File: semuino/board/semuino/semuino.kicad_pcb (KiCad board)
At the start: 2 copper layers, 115 x 77 mm, 34 parts, among them J1 bpc_pwr_10A, J10 Conn_01x02, J11 Conn_01x02, J12 Conn_01x02, J13 Conn_01x02, J2 bpc_pwr_10A, J3 bpc_pwr_5A, J4 bpc_pwr_5A, J5 bpc_pwr_5A, J6 bpc_pwr_5A, J7 Conn_01x03, J8 Conn_01x03, J9 Conn_01x03, Q1 TIP41C, Q2 TIP41C, Q3 TIP41C, Q4 TIP41C

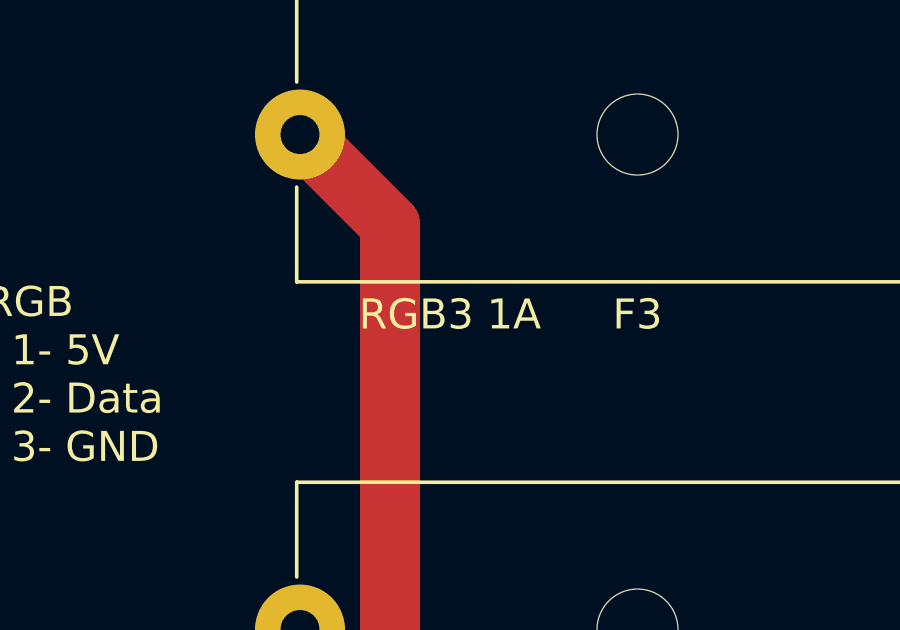
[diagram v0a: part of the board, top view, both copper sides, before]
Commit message: Erreur marquage fusible
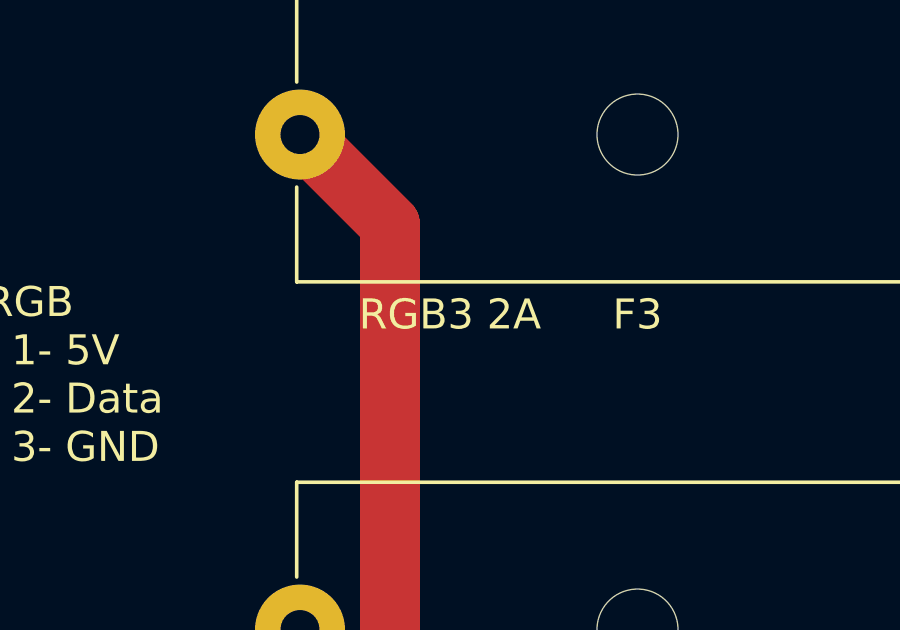
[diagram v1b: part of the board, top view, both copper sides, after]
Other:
- board text removed: "RGB3 1A"

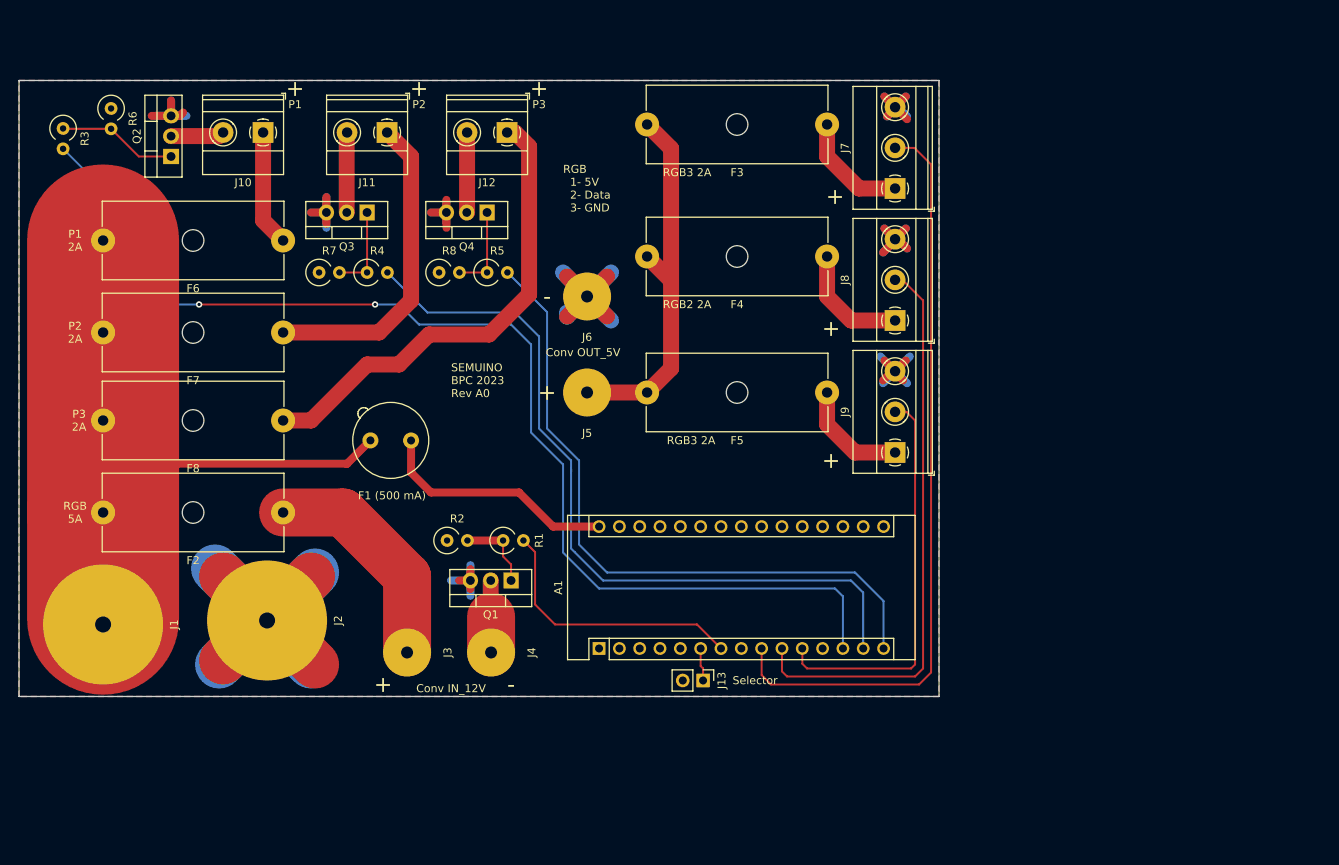
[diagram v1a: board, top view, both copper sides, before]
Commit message: Carte de commande éclairage semi
- Alim 12V/10A
- 3 sorties 12V/2A
- 3 sorties RGB 5V/2A
- RTC
- Sonde température
- extension ESP 01 Wifi
- 1 entrée select
- 1 entrée ON/OFF pour ESP 01
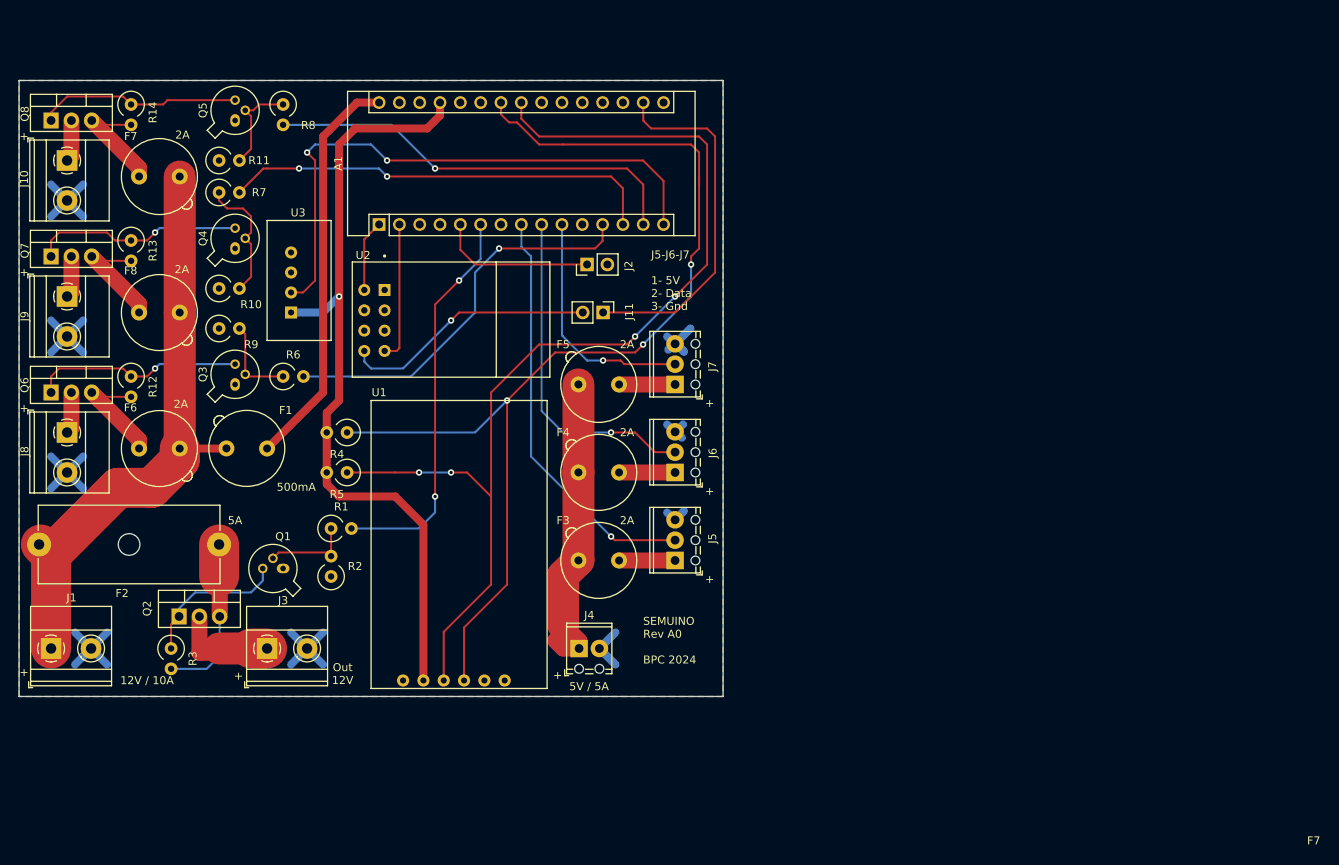
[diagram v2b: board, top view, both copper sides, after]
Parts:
- removed F1 (500 mA): 500mA, Fuse:Fuseholder_TR5_Littelfuse_No560_No460
- removed J12: Conn_01x02, TerminalBlock_Phoenix:TerminalBlock_Phoenix_MKDS-1,5-2_1x02_P5.00mm_Horizontal
- removed J13: Conn_01x02, Connector_PinHeader_2.54mm:PinHeader_1x02_P2.54mm_Vertical
- added ?: , , F.Cu at (88.8, 66.0)
- added F1: 500mA, Fuse:Fuseholder_TR5_Littelfuse_No560_No460, F.Cu at (106.0, 105.0)
- added Q5: 2N2222A, Package_TO_SOT_THT:TO-18-3, F.Cu at (102.0, 64.0)
- added Q6: P03P4L-04, Package_TO_SOT_THT:TO-220-3_Vertical, F.Cu at (79.0, 98.0)
- added Q7: P03P4L-04, Package_TO_SOT_THT:TO-220-3_Vertical, F.Cu at (79.0, 81.0)
- added Q8: P03P4L-04, Package_TO_SOT_THT:TO-220-3_Vertical, F.Cu at (79.0, 64.0)
- added R10: 100k, Resistor_THT:R_Axial_DIN0309_L9.0mm_D3.2mm_P2.54mm_Vertical, F.Cu at (100.0, 85.0)
- added R11: 100k, Resistor_THT:R_Axial_DIN0309_L9.0mm_D3.2mm_P2.54mm_Vertical, F.Cu at (100.0, 69.0)
- added R12: 100, Resistor_THT:R_Axial_DIN0309_L9.0mm_D3.2mm_P2.54mm_Vertical, F.Cu at (89.0, 96.0)
- added R13: 100k, Resistor_THT:R_Axial_DIN0309_L9.0mm_D3.2mm_P2.54mm_Vertical, F.Cu at (89.0, 79.0)
- added R14: 100k, Resistor_THT:R_Axial_DIN0309_L9.0mm_D3.2mm_P2.54mm_Vertical, F.Cu at (89.0, 62.0)
- added R9: 100k, Resistor_THT:R_Axial_DIN0309_L9.0mm_D3.2mm_P2.54mm_Vertical, F.Cu at (100.0, 90.0)
- added U1: RtcArduino, bpc:BPC_RtcArduino, F.Cu at (123.0, 134.0)
- added U2: BPC_ESP8266-01_ESP-01, bpc:BPC_XCVR_ESP8266-01_ESP-01, F.Cu at (129.0, 89.0)
- added U3: BPC_DHT22, bpc:BPC_DHT22, F.Cu at (109.0, 88.0)
- A1: value Arduino_Nano_v3.x -> Arduino_Nano_v2.x
- F3, F4, F5, F6, F7, F8: footprint Fuse:Fuseholder_Cylinder-5x20mm_Schurter_0031_8201_Horizontal_Open -> Fuse:Fuseholder_TR5_Littelfuse_No560_No460
- J1: value bpc_pwr_10A -> Conn_01x02; footprint bpc:BPC_PWR_10A -> TerminalBlock_Phoenix:TerminalBlock_Phoenix_MKDS-1,5-2_1x02_P5.00mm_Horizontal
- J11: footprint TerminalBlock_Phoenix:TerminalBlock_Phoenix_MKDS-1,5-2_1x02_P5.00mm_Horizontal -> Connector_PinHeader_2.54mm:PinHeader_1x02_P2.54mm_Vertical
- J2: value bpc_pwr_10A -> Conn_01x02; footprint bpc:BPC_PWR_10A -> Connector_PinHeader_2.54mm:PinHeader_1x02_P2.54mm_Vertical
- J3: value bpc_pwr_5A -> Conn_01x02; footprint bpc:BPC_PWR_5A -> TerminalBlock_Phoenix:TerminalBlock_Phoenix_MKDS-1,5-2_1x02_P5.00mm_Horizontal
- J4: value bpc_pwr_5A -> Conn_01x02; footprint bpc:BPC_PWR_5A -> TerminalBlock_Phoenix:TerminalBlock_Phoenix_MPT-0,5-2-2.54_1x02_P2.54mm_Horizontal
- J5, J6: value bpc_pwr_5A -> Conn_01x03; footprint bpc:BPC_PWR_5A -> TerminalBlock_Phoenix:TerminalBlock_Phoenix_MPT-0,5-3-2.54_1x03_P2.54mm_Horizontal
- J7: footprint TerminalBlock_Phoenix:TerminalBlock_Phoenix_MKDS-1,5-3-5.08_1x03_P5.08mm_Horizontal -> TerminalBlock_Phoenix:TerminalBlock_Phoenix_MPT-0,5-3-2.54_1x03_P2.54mm_Horizontal
- J8, J9: value Conn_01x03 -> Conn_01x02; footprint TerminalBlock_Phoenix:TerminalBlock_Phoenix_MKDS-1,5-3-5.08_1x03_P5.08mm_Horizontal -> TerminalBlock_Phoenix:TerminalBlock_Phoenix_MKDS-1,5-2_1x02_P5.00mm_Horizontal
- Q1, Q3, Q4: value TIP41C -> 2N2222A; footprint Package_TO_SOT_THT:TO-220-3_Vertical -> Package_TO_SOT_THT:TO-18-3
- Q2: value TIP41C -> P03P4L-04
- R1: value 50 -> 100
- R3, R4, R5: value 100 -> 100k
- R6, R7, R8: value 100k -> 100
- moved J9 105.3 mm to (81.0, 86.0), turned to 270 degrees
- moved J8 104.4 mm to (81.0, 103.0), turned to 270 degrees
- moved R3 66.4 mm to (94.0, 130.0)
- moved F3 60.4 mm to (150.0, 119.0)
- moved J2 59.8 mm to (146.0, 82.0)
- moved A1 59.7 mm to (120.0, 77.0)
- moved Q2 57.5 mm to (95.0, 126.0), turned to 0 degrees
- moved R6 39.8 mm to (108.0, 96.0), turned to 0 degrees
- moved F4 37.5 mm to (150.0, 108.0)
- moved J7 36.8 mm to (157.0, 97.0)
- moved J11 35.1 mm to (148.0, 88.0), turned to 270 degrees
- moved Q4 31.8 mm to (102.0, 80.0), turned to 90 degrees
- moved F6 31.6 mm to (90.0, 105.0), turned to 0 degrees
- moved R5 30.5 mm to (116.0, 108.0), turned to 180 degrees
- moved R8 28.7 mm to (108.0, 62.0), turned to 270 degrees
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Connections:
- A1 pad 1: Net-(A1-Pad1) -> NanoTx
- A1 pad 10: CmdRGB2 -> CmdRGB3
- A1 pad 11: CmdRGB3 -> Net-(A1-Pad11)
- A1 pad 12: Net-(A1-Pad12) -> CmdP1
- A1 pad 13: CmdP1 -> CmdP2
- A1 pad 14: CmdP2 -> CmdP3
- A1 pad 15: CmdP3 -> Temp
- A1 pad 17: Net-(A1-Pad17) -> 3.3V
- A1 pad 2: Net-(A1-Pad2) -> NanoRX
- A1 pad 23: Net-(A1-Pad23) -> SDA
- A1 pad 24: Net-(A1-Pad24) -> SCL
- A1 pad 27: Net-(A1-Pad27) -> Vcc
- A1 pad 30: Net-(A1-Pad30) -> Vin
- A1 pad 5: Net-(A1-Pad5) -> SELECT
- A1 pad 6: SELECT -> CmdPWR5
- A1 pad 7: CmdPWR5 -> Net-(A1-Pad7)
- A1 pad 8: Net-(A1-Pad8) -> CmdRGB1
- A1 pad 9: CmdRGB1 -> CmdRGB2
- F3 pad 2: Net-(F3-Pad2) -> PWR_5V
- F4 pad 2: Net-(F3-Pad2) -> PWR_5V
- F5 pad 2: Net-(F3-Pad2) -> PWR_5V
- J10 pad 1: Net-(F6-Pad1) -> Net-(J10-Pad1)
- J10 pad 2: Net-(J10-Pad2) -> GND
- J11 pad 1: Net-(F7-Pad1) -> 3.3V
- J2 pad 1: GND -> SELECT
- J3 pad 1: Net-(F2-Pad1) -> Net-(J3-Pad1)
- J4 pad 1: Net-(J4-Pad1) -> PWR_5V
- J5 pad 1: Net-(F3-Pad2) -> Net-(F3-Pad1)
- J6 pad 1: GND -> Net-(F4-Pad1)
- J7 pad 1: Net-(F3-Pad1) -> Net-(F5-Pad1)
- J7 pad 2: CmdRGB1 -> CmdRGB3
- J8 pad 1: Net-(F4-Pad1) -> Net-(J8-Pad1)
- J8 pad 2: CmdRGB2 -> GND
- J9 pad 1: Net-(F5-Pad1) -> Net-(J9-Pad1)
- J9 pad 2: CmdRGB3 -> GND
- Q1 pad 1: Net-(Q1-Pad1) -> GND
- Q1 pad 2: Net-(J4-Pad1) -> Net-(Q1-Pad2)
- Q1 pad 3: GND -> Net-(Q1-Pad3)
- Q2 pad 1: Net-(Q2-Pad1) -> Net-(Q1-Pad3)
- Q2 pad 2: Net-(J10-Pad2) -> Net-(J3-Pad1)
- Q2 pad 3: GND -> Net-(F2-Pad1)
- Q3 pad 1: Net-(Q3-Pad1) -> GND
- Q3 pad 2: Net-(J11-Pad2) -> Net-(Q3-Pad2)
- Q3 pad 3: GND -> Net-(Q3-Pad3)
- Q4 pad 1: Net-(Q4-Pad1) -> GND
- Q4 pad 2: Net-(J12-Pad2) -> Net-(Q4-Pad2)
- Q4 pad 3: GND -> Net-(Q4-Pad3)
- R1 pad 1: Net-(Q1-Pad1) -> Net-(Q1-Pad2)
- R2 pad 2: Net-(Q1-Pad1) -> Net-(Q1-Pad2)
- R3 pad 1: Net-(Q2-Pad1) -> Net-(Q1-Pad3)
- R3 pad 2: CmdP1 -> Net-(F2-Pad1)
- R4 pad 1: Net-(Q3-Pad1) -> SCL
- R4 pad 2: CmdP2 -> Vcc
- R5 pad 1: Net-(Q4-Pad1) -> SDA
- R5 pad 2: CmdP3 -> Vcc
- R6 pad 1: GND -> Net-(Q3-Pad2)
- R6 pad 2: Net-(Q2-Pad1) -> CmdP1
- R7 pad 1: GND -> Net-(Q4-Pad2)
- R7 pad 2: Net-(Q3-Pad1) -> CmdP2
- R8 pad 1: GND -> Net-(Q5-Pad2)
- R8 pad 2: Net-(Q4-Pad1) -> CmdP3
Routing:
- net SCL: track 0.00 -> 134.9 mm, vias 0 -> 3
- net SDA: track 0.00 -> 132.9 mm, vias 0 -> 4
- net GND: track 186.9 -> 78.7 mm
- net Vcc: track 0.00 -> 99.3 mm, vias 0 -> 1
- net CmdP1: track 143.3 -> 49.4 mm, vias 2 -> 1
- net Temp: track 0.00 -> 72.3 mm, vias 0 -> 2
- net Vin: track 0.00 -> 50.7 mm
- net Net-(F3-Pad2): track 47.7 -> 0.00 mm
- net 3.3V: track 0.00 -> 45.1 mm
- net Net-(F8-Pad1): track 59.2 -> 14.6 mm
- net CmdRGB1: track 94.5 -> 51.8 mm, vias 0 -> 1
- net CmdP2: track 96.7 -> 54.7 mm, vias 0 -> 2
- net PWR_5V: track 0.00 -> 38.0 mm
- net CmdP3: track 84.6 -> 53.1 mm, vias 0 -> 1
- net Net-(A1-Pad30): track 30.3 -> 0.00 mm
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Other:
- board size 115 x 77 mm -> 88 x 77 mm
- board text added: "12V / 10A"
- board text added: "2A"
- board text added: "500mA"
- board text added: "5A"
- board text added: "5V / 5A"
- board text added: "J5-J6-J7 1- 5V 2- Data 3- Gnd"
- board text added: "Out 12V"
- board text added: "SEMUINO Rev A0 BPC 2024"
- board text removed: "-"
- board text removed: "Conv IN_12V"
- board text removed: "Conv OUT_5V"
- board text removed: "P1"
- board text removed: "P1 2A"
- board text removed: "P2"
- board text removed: "P2 2A"
- board text removed: "P3"
- board text removed: "P3 2A"
- board text removed: "RGB 1- 5V 2- Data 3- GND"
- board text removed: "RGB 5A"
- board text removed: "RGB2 2A"
- board text removed: "RGB3 2A"
- board text removed: "SEMUINO BPC 2023 Rev A0"
- board text removed: "Selector"

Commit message: SEMUINO: Rework de la carte
- 3 LEDs 12V
- 3 LEDs RGB (avec R de protection sur data)
- 3 capteurs humidité sol
- 1 Connecteur pour écran OLED
- 1 RTC
- 1 ESP01 pour le Wifi
- Des fusibles
- carte au format boîte de dérivation
- ...
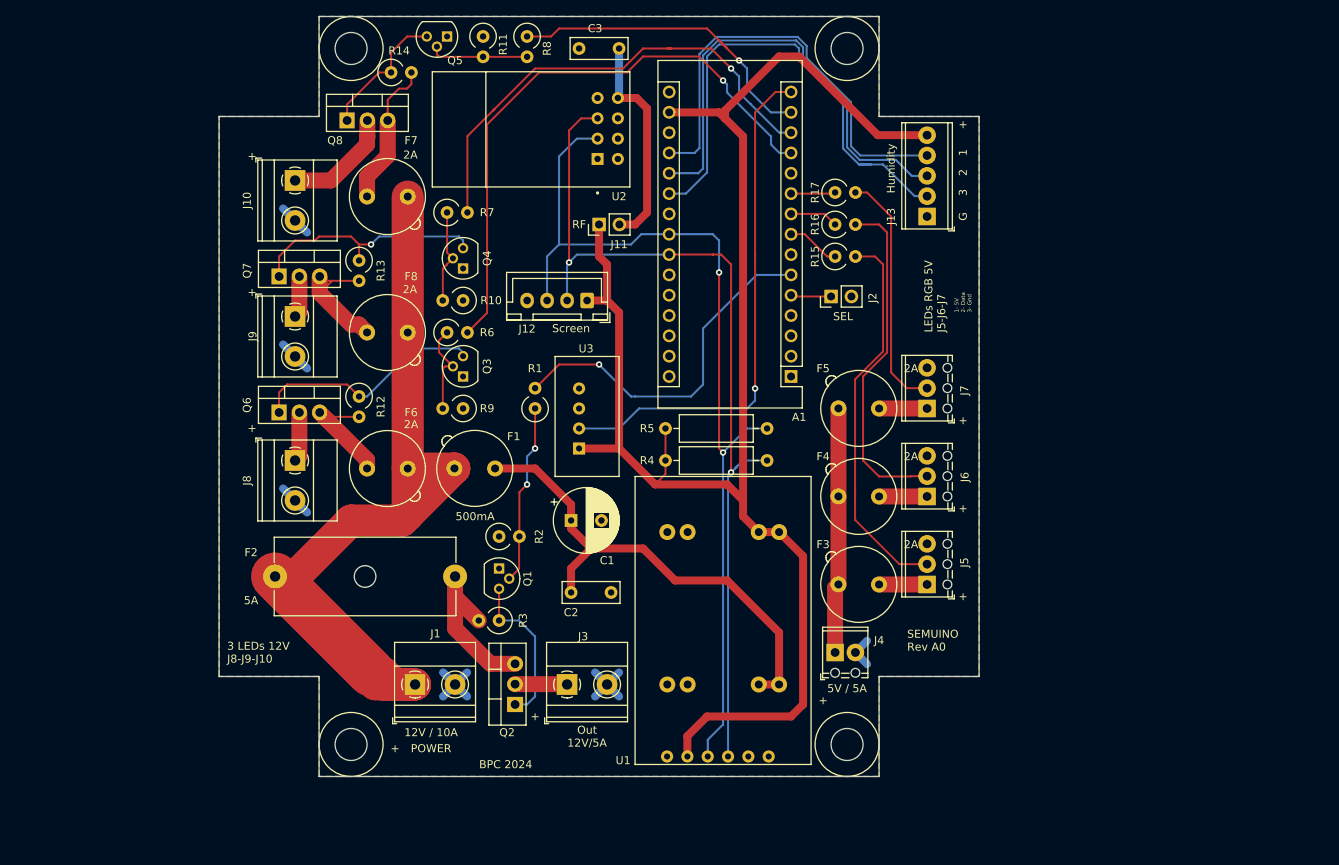
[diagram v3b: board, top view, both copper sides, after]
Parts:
- removed the ? at (88.8, 66.0)
- added ?: , , F.Cu at (193.5, 78.0)
- added ?: , , F.Cu at (193.5, 71.0)
- added ?: , , F.Cu at (57.3, 77.5)
- added C1: 20µF, Capacitor_THT:CP_Radial_D8.0mm_P3.80mm, F.Cu at (144.0, 114.0)
- added C2: 100nF, Capacitor_THT:C_Disc_D7.0mm_W2.5mm_P5.00mm, F.Cu at (144.0, 123.0)
- added C3: 100nF, Capacitor_THT:C_Disc_D7.0mm_W2.5mm_P5.00mm, F.Cu at (150.0, 55.0)
- added J12: Screen, Connector_JST:JST_XH_B4B-XH-A_1x04_P2.50mm_Vertical, F.Cu at (146.0, 86.5)
- added J13: Earth humidity sensor, TerminalBlock_Phoenix:TerminalBlock_Phoenix_MPT-0,5-5-2.54_1x05_P2.54mm_Horizontal, F.Cu at (188.5, 76.0)
- added R15: 100, Resistor_THT:R_Axial_DIN0309_L9.0mm_D3.2mm_P2.54mm_Vertical, F.Cu at (177.0, 81.0)
- added R16: 100, Resistor_THT:R_Axial_DIN0309_L9.0mm_D3.2mm_P2.54mm_Vertical, F.Cu at (177.0, 77.0)
- added R17: 100, Resistor_THT:R_Axial_DIN0309_L9.0mm_D3.2mm_P2.54mm_Vertical, F.Cu at (177.0, 73.0)
- added REF**: BPC_Trou4mm_Fixation, bpc:BPC_Trou4mm_Fixation, F.Cu at (116.5, 55.0)
- added REF**: BPC_Trou4mm_Fixation, bpc:BPC_Trou4mm_Fixation, F.Cu at (116.5, 142.0)
- added REF**: BPC_Trou4mm_Fixation, bpc:BPC_Trou4mm_Fixation, F.Cu at (178.5, 55.0)
- added REF**: BPC_Trou4mm_Fixation, bpc:BPC_Trou4mm_Fixation, F.Cu at (178.5, 142.0)
- added U4: BPC_Alim3_3V, bpc:BPC_Alim3_3V, B.Cu at (170.0, 134.5)
- J1: value Conn_01x02 -> 12V_POWER_IN
- J10: value Conn_01x02 -> POW LED 3
- J11: value Conn_01x02 -> RF ON/OFF
- J2: value Conn_01x02 -> Select
- J3: value Conn_01x02 -> 12V_POWER_OUT
- J4: value Conn_01x02 -> 5V_POWER_IN
- J5: value Conn_01x03 -> RGB 1
- J6: value Conn_01x03 -> RGB 2
- J7: value Conn_01x03 -> RGB 3
- J8: value Conn_01x02 -> POW LED 1
- J9: value Conn_01x02 -> POW LED 2
- Q1, Q3, Q4, Q5: footprint Package_TO_SOT_THT:TO-18-3 -> Package_TO_SOT_THT:TO-92
- R1, R6, R7, R8: value 100 -> 220
- R12: value 100 -> 100k
- R4, R5: value 100k -> 10k; footprint Resistor_THT:R_Axial_DIN0309_L9.0mm_D3.2mm_P2.54mm_Vertical -> Resistor_THT:R_Axial_DIN0309_L9.0mm_D3.2mm_P12.70mm_Horizontal
- moved A1 54.9 mm to (171.5, 96.0), turned to 180 degrees
- moved R5 52.8 mm to (168.5, 102.5)
- moved R4 52.6 mm to (168.5, 106.5)
- moved J1 45.7 mm to (124.5, 134.5)
- moved Q2 43.4 mm to (137.0, 137.0), turned to 90 degrees
- moved R3 41.1 mm to (135.0, 126.5), turned to 180 degrees
- moved U3 39.8 mm to (145.0, 105.0)
- moved J3 37.8 mm to (143.5, 134.5)
- moved Q8 37.0 mm to (116.0, 64.0)
- moved R11 36.5 mm to (133.0, 53.5), turned to 270 degrees
- moved U1 34.3 mm to (156.0, 143.5)
- moved R14 32.7 mm to (121.5, 58.0), turned to 0 degrees
- moved F3 32.6 mm to (182.5, 122.0)
- moved F4 32.6 mm to (182.5, 111.0)
- moved F5 32.6 mm to (182.5, 100.0)
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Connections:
- A1 pad 1: NanoTx -> Net-(A1-Pad1)
- A1 pad 19: Net-(A1-Pad19) -> Hum1
- A1 pad 2: NanoRX -> Net-(A1-Pad2)
- A1 pad 20: Net-(A1-Pad20) -> Hum2
- A1 pad 21: Net-(A1-Pad21) -> Hum3
- A1 pad 27: Vcc -> Net-(A1-Pad27)
- A1 pad 30: Vin -> Net-(A1-Pad30)
- J5 pad 2: CmdRGB1 -> Net-(J5-Pad2)
- J6 pad 2: CmdRGB2 -> Net-(J6-Pad2)
- J7 pad 2: CmdRGB3 -> Net-(J7-Pad2)
- R4 pad 2: Vcc -> 3.3V
- R5 pad 2: Vcc -> 3.3V
- R8 pad 1: Net-(Q5-Pad2) -> CmdP3
- R8 pad 2: CmdP3 -> Net-(Q5-Pad2)
- U1 pad 2: Vcc -> 3.3V
- U2 pad 2: Net-(U2-Pad2) -> SDA
- U2 pad 3: Net-(U2-Pad3) -> SCL
- U2 pad 4: NanoRX -> Net-(U2-Pad4)
- U2 pad 5: NanoTx -> Net-(U2-Pad5)
- U3 pad 1: Vcc -> 3.3V
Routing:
- net 3.3V: track 45.1 -> 200.1 mm
- net Vcc: track 99.3 -> 0.00 mm, vias 1 -> 0
- net Hum3: track 0.00 -> 61.9 mm
- net Hum2: track 0.00 -> 58.5 mm
- net Hum1: track 0.00 -> 55.4 mm
- net Net-(J5-Pad2): track 0.00 -> 49.0 mm
- net CmdRGB1: track 51.8 -> 6.65 mm, vias 1 -> 0
- net GND: track 78.7 -> 33.8 mm
- net Net-(J6-Pad2): track 0.00 -> 43.0 mm
- net CmdRGB2: track 42.1 -> 6.05 mm, vias 1 -> 0
- net Net-(F1-Pad2): track 75.8 -> 107.3 mm
- net Net-(J7-Pad2): track 0.00 -> 30.5 mm
- net CmdP1: track 49.4 -> 75.2 mm
- net CmdRGB3: track 29.5 -> 5.56 mm, vias 1 -> 0
- net SCL: track 134.9 -> 113.9 mm, vias 3 -> 2
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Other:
- board size 88 x 77 mm -> 95 x 95 mm
- board text added: "1"
- board text added: "1- 5V 2- Data 3- Gnd"
- board text added: "2"
- board text added: "3"
- board text added: "3 LEDs 12V J8-J9-J10"
- board text added: "BPC 2024"
- board text added: "G"
- board text added: "Humidity"
- board text added: "LEDs RGB 5V J5-J6-J7"
- board text added: "Out 12V/5A"
- board text added: "POWER"
- board text added: "RF"
- board text added: "SEL"
- board text added: "SEMUINO Rev A0"
- board text added: "Screen"
- board text removed: "J5-J6-J7 1- 5V 2- Data 3- Gnd"
- board text removed: "Out 12V"
- board text removed: "SEMUINO Rev A0 BPC 2024"

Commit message: Passage kicat 7 + rework
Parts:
- added C4: 20µF, Capacitor_THT:CP_Radial_D8.0mm_P3.80mm, F.Cu at (148.2, 77.8)
- added J14: Select, Connector_PinHeader_2.54mm:PinHeader_1x02_P2.54mm_Vertical, F.Cu at (176.2, 86.8)
- F2: footprint Fuse:Fuseholder_Cylinder-5x20mm_Schurter_0031_8201_Horizontal_Open -> Fuse:Fuseholder_Clip-5x20mm_Littelfuse_520_Inline_P20.50x5.80mm_D1.30mm_Horizontal
- moved J11 9.79 mm to (151.2, 86.0), turned to 180 degrees
- moved J2 5.01 mm to (176.2, 91.0)
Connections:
- A1 pad 1: Net-(A1-Pad1) -> unconnected-(A1-D1/TX-Pad1)
- A1 pad 11: Net-(A1-Pad11) -> unconnected-(A1-D8-Pad11)
- A1 pad 16: Net-(A1-Pad16) -> unconnected-(A1-D13-Pad16)
- A1 pad 18: Net-(A1-Pad18) -> unconnected-(A1-AREF-Pad18)
- A1 pad 2: Net-(A1-Pad2) -> unconnected-(A1-D0/RX-Pad2)
- A1 pad 22: Net-(A1-Pad22) -> unconnected-(A1-A3-Pad22)
- A1 pad 25: Net-(A1-Pad25) -> unconnected-(A1-A6-Pad25)
- A1 pad 26: Net-(A1-Pad26) -> unconnected-(A1-A7-Pad26)
- A1 pad 27: Net-(A1-Pad27) -> unconnected-(A1-+5V-Pad27)
- A1 pad 28: Net-(A1-Pad28) -> unconnected-(A1-~{RESET}-Pad28)
- A1 pad 3: Net-(A1-Pad3) -> unconnected-(A1-~{RESET}-Pad3)
- A1 pad 30: Net-(A1-Pad30) -> unconnected-(A1-VIN-Pad30)
- A1 pad 7: Net-(A1-Pad7) -> SELECT2
- U1 pad 5: Net-(U1-Pad5) -> unconnected-(U1-SQW-Pad5)
- U1 pad 6: Net-(U1-Pad6) -> unconnected-(U1-32K-Pad6)
- U2 pad 4: Net-(U2-Pad4) -> unconnected-(U2-RXD-Pad4)
- U2 pad 5: Net-(U2-Pad5) -> unconnected-(U2-TXD-Pad5)
- U2 pad 6: Net-(U2-Pad6) -> unconnected-(U2-EN-Pad6)
- U2 pad 7: Net-(U2-Pad7) -> unconnected-(U2-~{RST}-Pad7)
- U3 pad 3: Net-(U3-Pad3) -> unconnected-(U3-NC-Pad3)
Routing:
- net SDA: track 117.5 -> 126.4 mm
- net Net-(Q2-S): track 20.0 -> 28.9 mm
- net SELECT2: track 0.00 -> 8.83 mm
- net Net-(J1-Pin_1): track 107.3 -> 99.3 mm
- net Net-(J11-Pin_2): track 27.5 -> 34.9 mm
- net 3.3V: track 200.1 -> 193.0 mm
- net SCL: track 113.9 -> 119.2 mm
- net SELECT: track 5.07 -> 9.14 mm
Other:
- net class Default removed
- board text added: "SEL 2"
